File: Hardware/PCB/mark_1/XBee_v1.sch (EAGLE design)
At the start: 17 parts, among them IC1 4050, IC2 LM1117S

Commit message: 
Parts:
- renumbered U$1 to IC3
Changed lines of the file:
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@@
 <part name="R1" library="mark_1" deviceset="R-EU_" device="R0805"/>
 <part name="D1" library="mark_1" deviceset="S1M" device=""/>
-<part name="U$1" library="mark_1" deviceset="XBEE-1" device="B1"/>
+<part name="IC3" library="mark_1" deviceset="XBEE-1" device="B1"/>
 <part name="GND2" library="mark_1" deviceset="GND" device=""/>
 <part name="+3V1" library="mark_1" deviceset="+3V3" device=""/>
@@
 <instances>
 <instance part="IC1" gate="D" x="22.86" y="2.54"/>
-<instance part="C1" gate="G$1" x="73.66" y="86.36" rot="R180"/>
+<instance part="C1" gate="G$1" x="73.66" y="86.36" smashed="yes" rot="R180">
+<attribute name="NAME" x="79.756" y="85.979" size="1.778" layer="95" rot="R180"/>
+<attribute name="VALUE" x="82.296" y="91.059" size="1.778" layer="96" rot="R180"/>
+</instance>
 <instance part="IC2" gate="G$1" x="30.48" y="91.44"/>
 <instance part="LED1" gate="G$1" x="43.18" y="30.48"/>
 <instance part="R1" gate="G$1" x="43.18" y="38.1" rot="R90"/>
 <instance part="D1" gate="D1" x="15.24" y="91.44"/>
-<instance part="U$1" gate="G$1" x="76.2" y="48.26"/>
+<instance part="IC3" gate="G$1" x="76.2" y="48.26"/>
 <instance part="GND2" gate="1" x="30.48" y="76.2"/>
 <instance part="+3V1" gate="G$1" x="43.18" y="99.06"/>
@@
 <instance part="+3V3" gate="G$1" x="66.04" y="96.52"/>
 <instance part="GND6" gate="1" x="66.04" y="76.2"/>
-<instance part="JP2" gate="G$1" x="0" y="60.96" rot="R180"/>
-<instance part="JP3" gate="G$1" x="0" y="53.34" rot="R180"/>
-<instance part="JP4" gate="G$1" x="0" y="40.64" rot="R180"/>
-<instance part="JP5" gate="G$1" x="0" y="30.48" rot="R180"/>
-<instance part="JP6" gate="G$1" x="0" y="17.78" rot="R180"/>
-<instance part="JP7" gate="G$1" x="0" y="10.16" rot="R180"/>
-<instance part="JP8" gate="G$1" x="0" y="2.54" rot="R180"/>
+<instance part="JP2" gate="G$1" x="-2.54" y="60.96" smashed="yes" rot="R180"/>
+<instance part="JP3" gate="G$1" x="-2.54" y="53.34" smashed="yes" rot="R180"/>
+<instance part="JP4" gate="G$1" x="-2.54" y="40.64" smashed="yes" rot="R180"/>
+<instance part="JP5" gate="G$1" x="-2.54" y="30.48" smashed="yes" rot="R180"/>
+<instance part="JP6" gate="G$1" x="-2.54" y="17.78" smashed="yes" rot="R180"/>
+<instance part="JP7" gate="G$1" x="-2.54" y="10.16" smashed="yes" rot="R180"/>
+<instance part="JP8" gate="G$1" x="-2.54" y="2.54" smashed="yes" rot="R180"/>
 <instance part="IC1" gate="A" x="22.86" y="17.78"/>
 <instance part="IC1" gate="B" x="22.86" y="40.64"/>
@@
 </segment>
 <segment>
-<pinref part="U$1" gate="G$1" pin="GND"/>
+<pinref part="IC3" gate="G$1" pin="GND"/>
 <pinref part="GND4" gate="1" pin="GND"/>
 <wire x1="53.34" y1="33.02" x2="53.34" y2="35.56" width="0.1524" layer="91"/>
@@
 </segment>
 <segment>
-<pinref part="U$1" gate="G$1" pin="VDD"/>
+<pinref part="IC3" gate="G$1" pin="VDD"/>
 <pinref part="+3V2" gate="G$1" pin="+3V3"/>
 <wire x1="55.88" y1="58.42" x2="53.34" y2="58.42" width="0.1524" layer="91"/>
@@
 <net name="N$3" class="0">
 <segment>
-<pinref part="U$1" gate="G$1" pin="DIN"/>
+<pinref part="IC3" gate="G$1" pin="DIN"/>
 <wire x1="33.02" y1="53.34" x2="55.88" y2="53.34" width="0.1524" layer="91"/>
 <pinref part="IC1" gate="C" pin="O"/>
@@
 <wire x1="33.02" y1="40.64" x2="35.56" y2="40.64" width="0.1524" layer="91"/>
 <wire x1="35.56" y1="40.64" x2="35.56" y2="48.26" width="0.1524" layer="91"/>
-<pinref part="U$1" gate="G$1" pin="RESET"/>
+<pinref part="IC3" gate="G$1" pin="RESET"/>
 <wire x1="35.56" y1="48.26" x2="55.88" y2="48.26" width="0.1524" layer="91"/>
 <pinref part="IC1" gate="B" pin="O"/>
@@
 <net name="RSSI" class="0">
 <segment>
-<pinref part="U$1" gate="G$1" pin="RSSI"/>
+<pinref part="IC3" gate="G$1" pin="RSSI"/>
 <pinref part="R1" gate="G$1" pin="2"/>
 <wire x1="55.88" y1="45.72" x2="43.18" y2="45.72" width="0.1524" layer="91"/>
@@
 <wire x1="43.18" y1="45.72" x2="38.1" y2="45.72" width="0.1524" layer="91"/>
 <wire x1="38.1" y1="45.72" x2="38.1" y2="30.48" width="0.1524" layer="91"/>
-<wire x1="38.1" y1="30.48" x2="2.54" y2="30.48" width="0.1524" layer="91"/>
-<label x="2.54" y="30.48" size="1.778" layer="95"/>
+<wire x1="38.1" y1="30.48" x2="0" y2="30.48" width="0.1524" layer="91"/>
+<label x="5.08" y="30.48" size="1.778" layer="95"/>
 <pinref part="JP5" gate="G$1" pin="1"/>
 </segment>
@@
 <wire x1="33.02" y1="17.78" x2="48.26" y2="17.78" width="0.1524" layer="91"/>
 <wire x1="48.26" y1="17.78" x2="48.26" y2="38.1" width="0.1524" layer="91"/>
-<pinref part="U$1" gate="G$1" pin="DTR"/>
+<pinref part="IC3" gate="G$1" pin="DTR"/>
 <wire x1="48.26" y1="38.1" x2="55.88" y2="38.1" width="0.1524" layer="91"/>
 <pinref part="IC1" gate="A" pin="O"/>
@@
 <net name="N$8" class="0">
 <segment>
-<pinref part="U$1" gate="G$1" pin="RTS"/>
+<pinref part="IC3" gate="G$1" pin="RTS"/>
 <wire x1="96.52" y1="48.26" x2="109.22" y2="48.26" width="0.1524" layer="91"/>
 <wire x1="109.22" y1="48.26" x2="109.22" y2="2.54" width="0.1524" layer="91"/>
@@
 <net name="N$10" class="0">
 <segment>
-<pinref part="U$1" gate="G$1" pin="DIO5"/>
+<pinref part="IC3" gate="G$1" pin="DIO5"/>
 <pinref part="R2" gate="G$1" pin="2"/>
 <wire x1="96.52" y1="45.72" x2="104.14" y2="45.72" width="0.1524" layer="91"/>
@@
 <net name="RXD" class="0">
 <segment>
-<wire x1="12.7" y1="53.34" x2="2.54" y2="53.34" width="0.1524" layer="91"/>
-<label x="2.54" y="53.34" size="1.778" layer="95"/>
+<wire x1="12.7" y1="53.34" x2="0" y2="53.34" width="0.1524" layer="91"/>
+<label x="5.08" y="53.34" size="1.778" layer="95"/>
 <pinref part="JP3" gate="G$1" pin="1"/>
 <pinref part="IC1" gate="C" pin="I"/>
@@
 <net name="RESET" class="0">
 <segment>
-<wire x1="12.7" y1="40.64" x2="2.54" y2="40.64" width="0.1524" layer="91"/>
-<label x="2.54" y="40.64" size="1.778" layer="95"/>
+<wire x1="12.7" y1="40.64" x2="0" y2="40.64" width="0.1524" layer="91"/>
+<label x="5.08" y="40.64" size="1.778" layer="95"/>
 <pinref part="JP4" gate="G$1" pin="1"/>
 <pinref part="IC1" gate="B" pin="I"/>
@@
 <net name="DTR" class="0">
 <segment>
-<wire x1="12.7" y1="17.78" x2="2.54" y2="17.78" width="0.1524" layer="91"/>
-<label x="2.54" y="17.78" size="1.778" layer="95"/>
+<wire x1="12.7" y1="17.78" x2="0" y2="17.78" width="0.1524" layer="91"/>
+<label x="5.08" y="17.78" size="1.778" layer="95"/>
 <pinref part="JP6" gate="G$1" pin="1"/>
 <pinref part="IC1" gate="A" pin="I"/>
@@
 <segment>
 <pinref part="IC1" gate="D" pin="I"/>
-<wire x1="12.7" y1="2.54" x2="2.54" y2="2.54" width="0.1524" layer="91"/>
-<label x="2.54" y="2.54" size="1.778" layer="95"/>
+<wire x1="12.7" y1="2.54" x2="0" y2="2.54" width="0.1524" layer="91"/>
+<label x="5.08" y="2.54" size="1.778" layer="95"/>
 <pinref part="JP8" gate="G$1" pin="1"/>
 </segment>
@@
 <net name="TXD" class="0">
 <segment>
-<pinref part="U$1" gate="G$1" pin="DOUT"/>
+<pinref part="IC3" gate="G$1" pin="DOUT"/>
 <wire x1="55.88" y1="55.88" x2="35.56" y2="55.88" width="0.1524" layer="91"/>
 <wire x1="35.56" y1="55.88" x2="35.56" y2="60.96" width="0.1524" layer="91"/>
-<wire x1="35.56" y1="60.96" x2="2.54" y2="60.96" width="0.1524" layer="91"/>
-<label x="2.54" y="60.96" size="1.778" layer="95"/>
+<wire x1="35.56" y1="60.96" x2="0" y2="60.96" width="0.1524" layer="91"/>
+<label x="5.08" y="60.96" size="1.778" layer="95"/>
 <pinref part="JP2" gate="G$1" pin="1"/>
 </segment>
@@
 <net name="CTS" class="0">
 <segment>
-<pinref part="U$1" gate="G$1" pin="CTS"/>
+<pinref part="IC3" gate="G$1" pin="CTS"/>
 <wire x1="96.52" y1="38.1" x2="99.06" y2="38.1" width="0.1524" layer="91"/>
 <wire x1="99.06" y1="38.1" x2="99.06" y2="10.16" width="0.1524" layer="91"/>
-<wire x1="99.06" y1="10.16" x2="2.54" y2="10.16" width="0.1524" layer="91"/>
-<label x="2.54" y="10.16" size="1.778" layer="95"/>
+<wire x1="99.06" y1="10.16" x2="0" y2="10.16" width="0.1524" layer="91"/>
+<label x="5.08" y="10.16" size="1.778" layer="95"/>
 <pinref part="JP7" gate="G$1" pin="1"/>
 </segment>

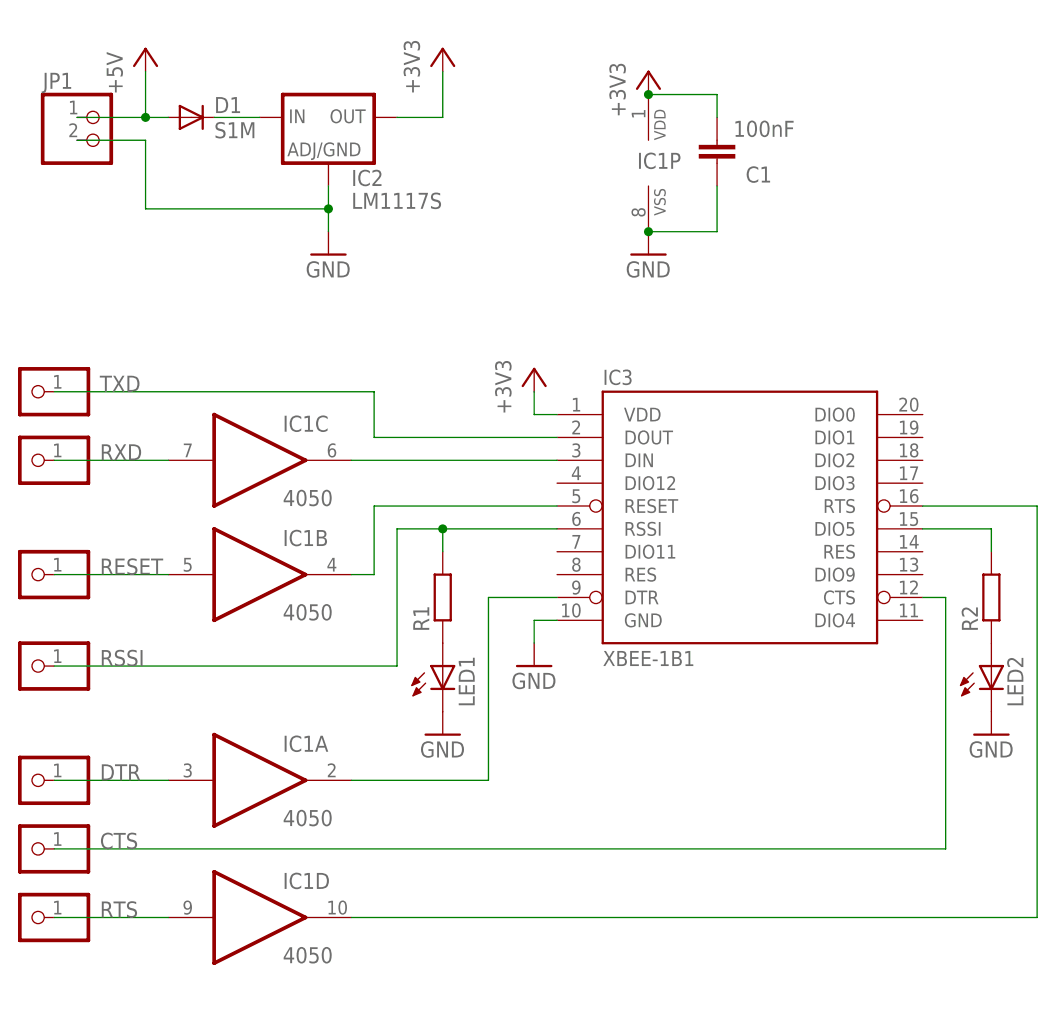
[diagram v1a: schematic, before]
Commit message: 
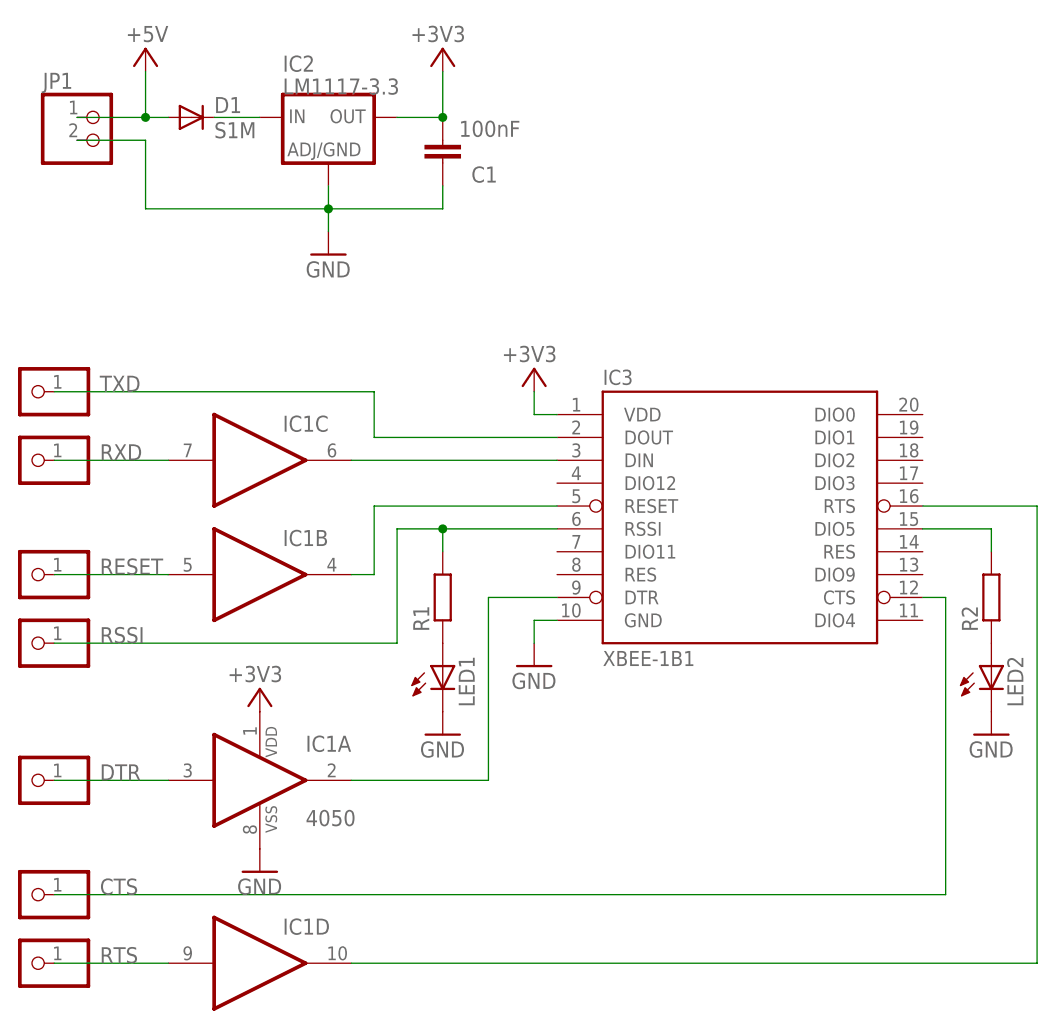
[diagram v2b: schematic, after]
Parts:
- IC2: value LM1117S -> LM1117-3.3
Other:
- moved on the sheet: C1, IC1D
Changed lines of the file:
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@@
 <part name="IC1" library="mark_1" deviceset="4050" device="D" value="4050"/>
 <part name="C1" library="mark_1" deviceset="C-EU" device="C0805K" value="100nF"/>
-<part name="IC2" library="mark_1" deviceset="LM1117" device="S"/>
+<part name="IC2" library="mark_1" deviceset="LM1117" device="S" value="LM1117-3.3"/>
 <part name="LED1" library="mark_1" deviceset="LED" device="3MM"/>
 <part name="R1" library="mark_1" deviceset="R-EU_" device="R0805"/>
@@
 </plain>
 <instances>
-<instance part="IC1" gate="D" x="22.86" y="2.54"/>
-<instance part="C1" gate="G$1" x="73.66" y="86.36" smashed="yes" rot="R180">
-<attribute name="NAME" x="79.756" y="85.979" size="1.778" layer="95" rot="R180"/>
-<attribute name="VALUE" x="82.296" y="91.059" size="1.778" layer="96" rot="R180"/>
-</instance>
-<instance part="IC2" gate="G$1" x="30.48" y="91.44"/>
+<instance part="IC1" gate="D" x="22.86" y="-2.54" smashed="yes">
+<attribute name="NAME" x="25.4" y="0.635" size="1.778" layer="95"/>
+</instance>
+<instance part="C1" gate="G$1" x="43.18" y="86.36" smashed="yes" rot="R180">
+<attribute name="NAME" x="49.276" y="85.979" size="1.778" layer="95" rot="R180"/>
+<attribute name="VALUE" x="51.816" y="91.059" size="1.778" layer="96" rot="R180"/>
+</instance>
+<instance part="IC2" gate="G$1" x="30.48" y="91.44" smashed="yes">
+<attribute name="NAME" x="25.4" y="96.52" size="1.778" layer="95"/>
+<attribute name="VALUE" x="25.4" y="93.98" size="1.778" layer="96"/>
+</instance>
 <instance part="LED1" gate="G$1" x="43.18" y="30.48"/>
 <instance part="R1" gate="G$1" x="43.18" y="38.1" rot="R90"/>
@@
 <instance part="IC3" gate="G$1" x="76.2" y="48.26"/>
 <instance part="GND2" gate="1" x="30.48" y="76.2"/>
-<instance part="+3V1" gate="G$1" x="43.18" y="99.06"/>
-<instance part="P+1" gate="1" x="10.16" y="99.06"/>
+<instance part="+3V1" gate="G$1" x="43.18" y="99.06" smashed="yes">
+<attribute name="VALUE" x="45.72" y="101.6" size="1.778" layer="96" rot="R180"/>
+</instance>
+<instance part="P+1" gate="1" x="10.16" y="99.06" smashed="yes">
+<attribute name="VALUE" x="12.7" y="101.6" size="1.778" layer="96" rot="R180"/>
+</instance>
 <instance part="JP1" gate="G$1" x="5.08" y="88.9"/>
-<instance part="+3V2" gate="G$1" x="53.34" y="63.5"/>
+<instance part="+3V2" gate="G$1" x="53.34" y="63.5" smashed="yes">
+<attribute name="VALUE" x="55.88" y="66.04" size="1.778" layer="96" rot="R180"/>
+</instance>
 <instance part="GND3" gate="1" x="43.18" y="22.86"/>
 <instance part="GND4" gate="1" x="53.34" y="30.48"/>
@@
 <instance part="LED2" gate="G$1" x="104.14" y="30.48"/>
 <instance part="GND5" gate="1" x="104.14" y="22.86"/>
-<instance part="IC1" gate="P" x="66.04" y="86.36"/>
-<instance part="+3V3" gate="G$1" x="66.04" y="96.52"/>
-<instance part="GND6" gate="1" x="66.04" y="76.2"/>
+<instance part="IC1" gate="P" x="22.86" y="17.78" smashed="yes"/>
+<instance part="+3V3" gate="G$1" x="22.86" y="27.94" smashed="yes">
+<attribute name="VALUE" x="25.4" y="30.48" size="1.778" layer="96" rot="R180"/>
+</instance>
+<instance part="GND6" gate="1" x="22.86" y="7.62"/>
 <instance part="JP2" gate="G$1" x="-2.54" y="60.96" smashed="yes" rot="R180"/>
 <instance part="JP3" gate="G$1" x="-2.54" y="53.34" smashed="yes" rot="R180"/>
 <instance part="JP4" gate="G$1" x="-2.54" y="40.64" smashed="yes" rot="R180"/>
-<instance part="JP5" gate="G$1" x="-2.54" y="30.48" smashed="yes" rot="R180"/>
+<instance part="JP5" gate="G$1" x="-2.54" y="33.02" smashed="yes" rot="R180"/>
 <instance part="JP6" gate="G$1" x="-2.54" y="17.78" smashed="yes" rot="R180"/>
-<instance part="JP7" gate="G$1" x="-2.54" y="10.16" smashed="yes" rot="R180"/>
-<instance part="JP8" gate="G$1" x="-2.54" y="2.54" smashed="yes" rot="R180"/>
-<instance part="IC1" gate="A" x="22.86" y="17.78"/>
-<instance part="IC1" gate="B" x="22.86" y="40.64"/>
-<instance part="IC1" gate="C" x="22.86" y="53.34"/>
+<instance part="JP7" gate="G$1" x="-2.54" y="5.08" smashed="yes" rot="R180"/>
+<instance part="JP8" gate="G$1" x="-2.54" y="-2.54" smashed="yes" rot="R180"/>
+<instance part="IC1" gate="A" x="22.86" y="17.78" smashed="yes">
+<attribute name="NAME" x="27.94" y="20.955" size="1.778" layer="95"/>
+<attribute name="VALUE" x="27.94" y="12.7" size="1.778" layer="96"/>
+</instance>
+<instance part="IC1" gate="B" x="22.86" y="40.64" smashed="yes">
+<attribute name="NAME" x="25.4" y="43.815" size="1.778" layer="95"/>
+</instance>
+<instance part="IC1" gate="C" x="22.86" y="53.34" smashed="yes">
+<attribute name="NAME" x="25.4" y="56.515" size="1.778" layer="95"/>
+</instance>
 </instances>
 <busses>
@@
 <wire x1="10.16" y1="88.9" x2="10.16" y2="81.28" width="0.1524" layer="91"/>
 <wire x1="10.16" y1="81.28" x2="30.48" y2="81.28" width="0.1524" layer="91"/>
+<pinref part="C1" gate="G$1" pin="1"/>
+<wire x1="30.48" y1="81.28" x2="43.18" y2="81.28" width="0.1524" layer="91"/>
+<wire x1="43.18" y1="81.28" x2="43.18" y2="83.82" width="0.1524" layer="91"/>
 </segment>
 <segment>
@@
 <pinref part="IC1" gate="P" pin="VSS"/>
 <pinref part="GND6" gate="1" pin="GND"/>
-<junction x="66.04" y="78.74"/>
-<pinref part="C1" gate="G$1" pin="1"/>
-<wire x1="66.04" y1="78.74" x2="73.66" y2="78.74" width="0.1524" layer="91"/>
-<wire x1="73.66" y1="78.74" x2="73.66" y2="83.82" width="0.1524" layer="91"/>
 </segment>
 </net>
@@
 <wire x1="38.1" y1="91.44" x2="43.18" y2="91.44" width="0.1524" layer="91"/>
 <wire x1="43.18" y1="91.44" x2="43.18" y2="96.52" width="0.1524" layer="91"/>
+<junction x="43.18" y="91.44"/>
+<pinref part="C1" gate="G$1" pin="2"/>
 </segment>
 <segment>
@@
 <pinref part="IC1" gate="P" pin="VDD"/>
 <pinref part="+3V3" gate="G$1" pin="+3V3"/>
-<junction x="66.04" y="93.98"/>
-<pinref part="C1" gate="G$1" pin="2"/>
-<wire x1="66.04" y1="93.98" x2="73.66" y2="93.98" width="0.1524" layer="91"/>
-<wire x1="73.66" y1="93.98" x2="73.66" y2="91.44" width="0.1524" layer="91"/>
 </segment>
 </net>
@@
 <junction x="43.18" y="45.72"/>
 <wire x1="43.18" y1="45.72" x2="38.1" y2="45.72" width="0.1524" layer="91"/>
-<wire x1="38.1" y1="45.72" x2="38.1" y2="30.48" width="0.1524" layer="91"/>
-<wire x1="38.1" y1="30.48" x2="0" y2="30.48" width="0.1524" layer="91"/>
-<label x="5.08" y="30.48" size="1.778" layer="95"/>
+<wire x1="38.1" y1="45.72" x2="38.1" y2="33.02" width="0.1524" layer="91"/>
+<wire x1="38.1" y1="33.02" x2="0" y2="33.02" width="0.1524" layer="91"/>
+<label x="5.08" y="33.02" size="1.778" layer="95"/>
 <pinref part="JP5" gate="G$1" pin="1"/>
 </segment>
@@
 <pinref part="IC3" gate="G$1" pin="RTS"/>
 <wire x1="96.52" y1="48.26" x2="109.22" y2="48.26" width="0.1524" layer="91"/>
-<wire x1="109.22" y1="48.26" x2="109.22" y2="2.54" width="0.1524" layer="91"/>
+<wire x1="109.22" y1="48.26" x2="109.22" y2="-2.54" width="0.1524" layer="91"/>
 <pinref part="IC1" gate="D" pin="O"/>
-<wire x1="109.22" y1="2.54" x2="33.02" y2="2.54" width="0.1524" layer="91"/>
+<wire x1="109.22" y1="-2.54" x2="33.02" y2="-2.54" width="0.1524" layer="91"/>
 </segment>
 </net>
@@
 <segment>
 <pinref part="IC1" gate="D" pin="I"/>
-<wire x1="12.7" y1="2.54" x2="0" y2="2.54" width="0.1524" layer="91"/>
-<label x="5.08" y="2.54" size="1.778" layer="95"/>
+<wire x1="12.7" y1="-2.54" x2="0" y2="-2.54" width="0.1524" layer="91"/>
+<label x="5.08" y="-2.54" size="1.778" layer="95"/>
 <pinref part="JP8" gate="G$1" pin="1"/>
 </segment>
@@
 <pinref part="IC3" gate="G$1" pin="CTS"/>
 <wire x1="96.52" y1="38.1" x2="99.06" y2="38.1" width="0.1524" layer="91"/>
-<wire x1="99.06" y1="38.1" x2="99.06" y2="10.16" width="0.1524" layer="91"/>
-<wire x1="99.06" y1="10.16" x2="0" y2="10.16" width="0.1524" layer="91"/>
-<label x="5.08" y="10.16" size="1.778" layer="95"/>
+<wire x1="99.06" y1="38.1" x2="99.06" y2="5.08" width="0.1524" layer="91"/>
+<wire x1="99.06" y1="5.08" x2="0" y2="5.08" width="0.1524" layer="91"/>
+<label x="5.08" y="5.08" size="1.778" layer="95"/>
 <pinref part="JP7" gate="G$1" pin="1"/>
 </segment>
